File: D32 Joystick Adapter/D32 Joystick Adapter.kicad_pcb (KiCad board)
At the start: 2 copper layers, 48.9 x 40.6 mm, 16 parts, among them J1 Dragon 32, J2 Joystick, M1 Mounting, M2 Mounting, M3 Mounting, M4 Mounting, U1 4066

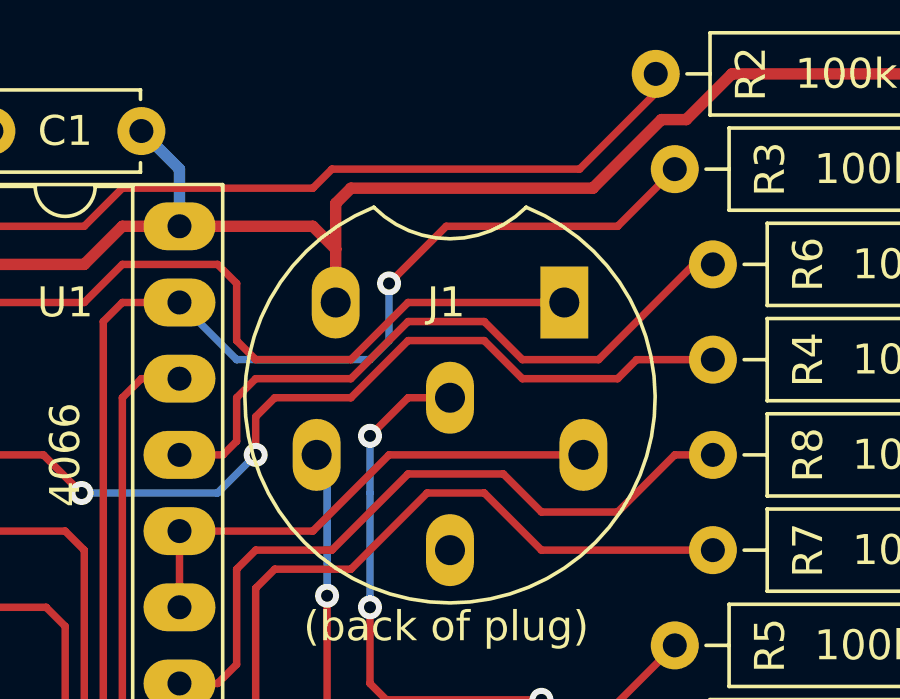
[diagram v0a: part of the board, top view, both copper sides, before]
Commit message: Added pinout to silkscreen
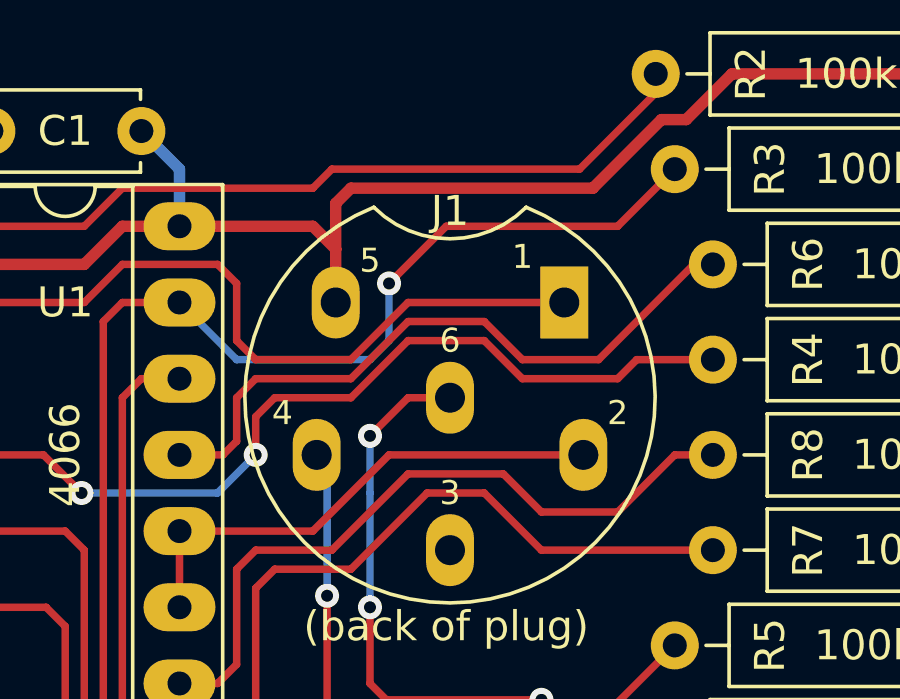
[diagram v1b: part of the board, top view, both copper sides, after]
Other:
- board text added: "(front of plug)"
- board text added: "1"
- board text added: "2"
- board text added: "3"
- board text added: "4"
- board text added: "5"
- board text added: "6"
- board text added: "J1 PINOUT: 1 POT_X 2 POT_Y 3 GND 4 /FIRE1 5 VCC 6 /FIRE2"
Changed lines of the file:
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@@
   (general
     (thickness 1.6)
-    (drawings 26)
+    (drawings 40)
     (tracks 179)
     (zones 0)
@@
     (descr "Through hole straight pin header, 1x04, 2.54mm pitch, single row")
     (tags "Through hole pin header THT 1x04 2.54mm single row")
-    (fp_text reference J1 (at 3.175 -0.127 180) (layer F.SilkS)
+    (fp_text reference J1 (at 6.223 0 180) (layer F.SilkS)
       (effects (font (size 1 1) (thickness 0.15)))
     )
@@
       (effects (font (size 1 1) (thickness 0.15)))
     )
+    (fp_arc (start 0 0) (end 6.349999 -2.539999) (angle -316.4) (layer B.SilkS) (width 0.12))
+    (fp_arc (start 8.89 0) (end 6.35 -2.539998) (angle -90) (layer B.SilkS) (width 0.12))
     (fp_arc (start 8.89 0) (end 6.35 -2.539998) (angle -89.99996616) (layer F.SilkS) (width 0.12))
     (fp_arc (start 0 0) (end 6.349999 -2.539999) (angle -316.397181) (layer F.SilkS) (width 0.12))
@@
     )
   )
+  (gr_text "J1 PINOUT:\n1 POT_X\n2 POT_Y\n3 GND\n4 /FIRE1\n5 VCC\n6 /FIRE2" (at 139.827 86.36) (layer B.SilkS)
+    (effects (font (size 0.8 0.8) (thickness 0.1)) (justify left mirror))
+  )
+  (gr_text 2 (at 128.27 86.868) (layer B.SilkS)
+    (effects (font (size 0.8 0.8) (thickness 0.1)) (justify mirror))
+  )
+  (gr_text 6 (at 122.682 84.455) (layer B.SilkS)
+    (effects (font (size 0.8 0.8) (thickness 0.1)) (justify mirror))
+  )
+  (gr_text 3 (at 122.682 89.535) (layer B.SilkS)
+    (effects (font (size 0.8 0.8) (thickness 0.1)) (justify mirror))
+  )
+  (gr_text 5 (at 120.015 81.788) (layer B.SilkS)
+    (effects (font (size 0.8 0.8) (thickness 0.1)) (justify mirror))
+  )
+  (gr_text 1 (at 125.095 81.661) (layer B.SilkS)
+    (effects (font (size 0.8 0.8) (thickness 0.1)) (justify mirror))
+  )
+  (gr_text 4 (at 117.094 86.868) (layer B.SilkS)
+    (effects (font (size 0.8 0.8) (thickness 0.1)) (justify mirror))
+  )
+  (gr_text "(front of plug)" (at 122.809 93.98) (layer B.SilkS)
+    (effects (font (size 1 1) (thickness 0.15)) (justify mirror))
+  )
+  (gr_text 4 (at 117.094 86.868) (layer F.SilkS)
+    (effects (font (size 0.8 0.8) (thickness 0.1)))
+  )
+  (gr_text 2 (at 128.27 86.868) (layer F.SilkS)
+    (effects (font (size 0.8 0.8) (thickness 0.1)))
+  )
+  (gr_text 5 (at 120.015 81.788) (layer F.SilkS)
+    (effects (font (size 0.8 0.8) (thickness 0.1)))
+  )
+  (gr_text 6 (at 122.682 84.455) (layer F.SilkS)
+    (effects (font (size 0.8 0.8) (thickness 0.1)))
+  )
+  (gr_text 3 (at 122.682 89.535) (layer F.SilkS)
+    (effects (font (size 0.8 0.8) (thickness 0.1)))
+  )
+  (gr_text 1 (at 125.095 81.661) (layer F.SilkS)
+    (effects (font (size 0.8 0.8) (thickness 0.1)))
+  )
   (gr_text "(back of plug)" (at 122.555 93.98) (layer F.SilkS)

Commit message: Added power jumper and changed resistor values
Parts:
- added JP1: PWR, Connector_PinHeader_2.54mm:PinHeader_1x02_P2.54mm_Horizontal, F.Cu at (141.0, 101.6)
- R1, R3, R5, R7: value 100k -> 10k
- R2, R4, R6, R8: value 100k -> 47k
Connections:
- J2 pad 5: Net-(J2-Pad5) -> (no net)
- J2 pad 7: VCC -> Net-(J2-Pad7)
- M1 pad 1: Net-(M1-Pad1) -> (no net)
- M2 pad 1: Net-(M2-Pad1) -> (no net)
- M3 pad 1: Net-(M3-Pad1) -> (no net)
- M4 pad 1: Net-(M4-Pad1) -> (no net)
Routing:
- net Net-(J2-Pad7): track 0.00 -> 28.8 mm, vias 0 -> 2
- net VCC: track 144.3 -> 143.4 mm, vias 1 -> 0
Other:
- board text added: "Revision B github.com/tebl"
- board text removed: "Revision A github.com/tebl"

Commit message: Added LICENSE text to PCB
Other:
- board text added: "Licensed under CERN OHL v1.2"
